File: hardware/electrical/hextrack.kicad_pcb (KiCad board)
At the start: 2 copper layers, 50.8 x 54.9 mm, 37 parts, among them SW1 B3U-1000P, U1 USBLC6-2SC6, U2 nRF52840, Y1 32 MHz Crystal

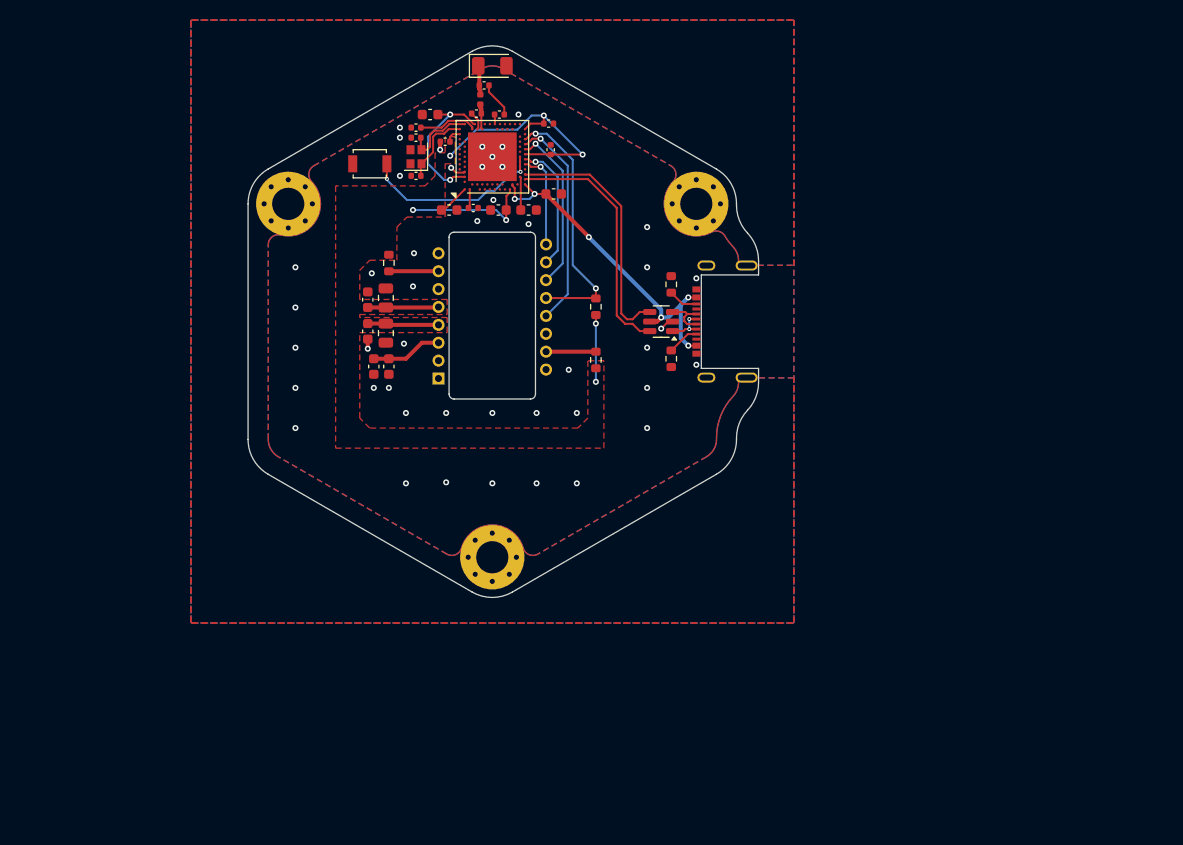
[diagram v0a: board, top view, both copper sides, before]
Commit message: Update schematic to include regulators and switches, update render
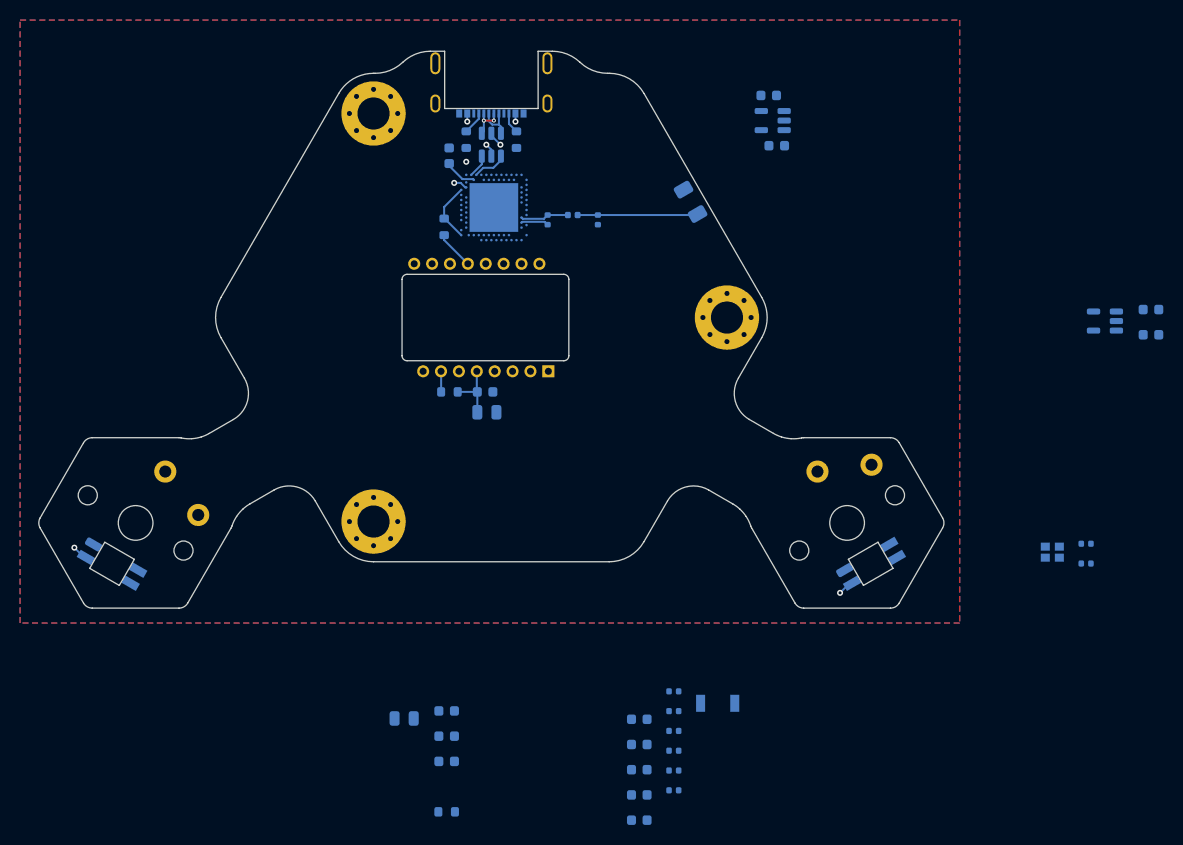
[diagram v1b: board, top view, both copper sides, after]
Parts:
- removed ANT1: Antenna, Diode_SMD:D_1206_3216Metric
- removed NS1: PMW3389DM-T3QU, HexTrack:PixArt_PMW3389DM-T3QU
- removed SW1: B3U-1000P, Button_Switch_SMD:SW_SPST_B3U-1000P
- removed USB1: USB Type-C Receptacle 16P, HexTrack:USB_C_16P_CB0.8_073
- added AN1: Antenna, Diode_SMD:D_1206_3216Metric, B.Cu at (168.3, 93.5)
- added C22: 10uF, Capacitor_SMD:C_0805_2012Metric, B.Cu at (148.1, 114.4)
- added C23: 10uF, Capacitor_SMD:C_0805_2012Metric, B.Cu at (139.8, 144.9)
- added C24: 100nF, Capacitor_SMD:C_0603_1608Metric, B.Cu at (144.1, 144.2)
- added C25: 100nF, Capacitor_SMD:C_0603_1608Metric, B.Cu at (144.1, 146.7)
- added C26: 4.7uF 10V, Capacitor_SMD:C_0603_1608Metric, B.Cu at (144.1, 149.2)
- added D1: SK6812MINI-E, ScottoKeebs_Components:LED_SK6812MINI, F.Cu at (110.8, 129.5)
- added D2: SK6812MINI-E, ScottoKeebs_Components:LED_SK6812MINI, F.Cu at (186.2, 129.5)
- added J1: USB Type-C Receptacle 16P, HexTrack:USB_C_16P_CB0.8_073, B.Cu at (148.5, 77.6)
- added S1: B3U-1000P, Button_Switch_SMD:SW_SPST_B3U-1000P, B.Cu at (171.0, 143.4)
- added S2: Kailh Choc V1, HexTrack:Choc_V1, F.Cu at (113.1, 125.4)
- added S3: Kailh Choc V1, HexTrack:Choc_V1, F.Cu at (183.9, 125.4)
- added U3: AP2204K-3.3, Package_TO_SOT_SMD:SOT-23-5, B.Cu at (209.6, 105.3)
- added U4: nRF52840, HexTrack:Nordic_AQFN-73-1EP_7x7mm_P0.5mm, B.Cu at (148.8, 94.0)
- added U5: PMW3389DM-T3QU, HexTrack:PixArt_PMW3389DM-T3QU, B.Cu at (148.5, 105.0)
- C1, C4: value 100nF -> 1uF; moved to B.Cu
- C10, C11, C14, C15, C19, L1, R3, U1, Y1: moved to B.Cu
- C12: value 100nF -> 4.7uF; footprint Capacitor_SMD:C_0402_1005Metric -> Capacitor_SMD:C_0603_1608Metric; moved to B.Cu
- C13: value 4.7uF -> 100nF; footprint Capacitor_SMD:C_0603_1608Metric -> Capacitor_SMD:C_0402_1005Metric; moved to B.Cu
- C16: value 4.7uF -> 1uF; moved to B.Cu
- C17: value 1uF -> 0.5pF; footprint Capacitor_SMD:C_0603_1608Metric -> Capacitor_SMD:C_0402_1005Metric; moved to B.Cu
- C18: value 12pF -> 0.8pF; moved to B.Cu
- C2, C3: value 10uF -> 1uF; footprint Capacitor_SMD:C_0805_2012Metric -> Capacitor_SMD:C_0603_1608Metric; moved to B.Cu
- C20: value 0.8pF -> 12pF; moved to B.Cu
- C21: value 0.5pF -> 100nF; footprint Capacitor_SMD:C_0402_1005Metric -> Capacitor_SMD:C_0603_1608Metric; moved to B.Cu
- C5: value 100nF -> 4.7uF; moved to B.Cu
- C6: value 4.7uF 10V -> 820pF; footprint Capacitor_SMD:C_0603_1608Metric -> Capacitor_SMD:C_0402_1005Metric; moved to B.Cu
- C7: value 100nF -> 100pF; moved to B.Cu
- C8: value 100pF -> 100nF; moved to B.Cu
- C9: value 820pF -> 4.7uF; footprint Capacitor_SMD:C_0402_1005Metric -> Capacitor_SMD:C_0603_1608Metric; moved to B.Cu
- R1: value 10k -> 5.1k; moved to B.Cu
- R2: value 13R -> 5.1k; moved to B.Cu
- R4: value 5.1k -> 13R; moved to B.Cu
- R5: value 5.1k -> 10k; moved to B.Cu
- U2: value nRF52840 -> AP2204K-1.8; footprint HexTrack:Nordic_AQFN-73-1EP_7x7mm_P0.5mm -> Package_TO_SOT_SMD:SOT-23-5; moved to B.Cu
- moved C4 77.9 mm to (214.1, 106.7), turned to 180 degrees
- moved C3 76.2 mm to (214.1, 104.2), turned to 180 degrees
- moved C19 76.1 mm to (207.7, 127.5)
- moved C20 75.4 mm to (207.7, 129.5), turned to 180 degrees
- moved Y1 74.6 mm to (204.3, 128.3), turned to 180 degrees
- moved C15 68.4 mm to (166.7, 152.1), turned to 180 degrees
- moved C11 68.4 mm to (163.2, 150.0), turned to 180 degrees
- moved C12 67.4 mm to (163.2, 152.5)
- moved C8 65.3 mm to (166.7, 146.1), turned to 180 degrees
- moved C14 63.0 mm to (166.7, 150.1), turned to 180 degrees
- moved C16 62.3 mm to (163.2, 155.0), turned to 180 degrees
- moved C9 61.8 mm to (163.2, 145.0)
- moved C13 56.7 mm to (166.7, 148.1)
- moved C10 54.3 mm to (163.2, 147.5)
- moved C7 53.9 mm to (166.7, 144.2)
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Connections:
- C1 pad 1: +1V8 -> GND
- C1 pad 2: GND -> VBUS
- C10 pad 2: Net-(U2-DECUSB) -> VBUS
- C11 pad 2: Net-(U2-DEC4) -> Net-(U4-DEC4)
- C12 pad 2: +1V8 -> /Block Diagram/MCU/VDD
- C13 pad 2: VBUS -> /Block Diagram/MCU/VDD
- C14 pad 2: +1V8 -> /Block Diagram/MCU/VDD
- C15 pad 2: +1V8 -> /Block Diagram/MCU/VDD
- C16 pad 2: +1V8 -> /Block Diagram/MCU/VDD
- C17 pad 2: +1V8 -> Net-(AN1-A)
- C18 pad 1: Net-(U2-XC1) -> RF_GND
- C18 pad 2: GND -> Net-(U4-ANT)
- C19 pad 1: Net-(U2-XC2) -> Net-(U4-XC1)
- C2 pad 1: +1V8 -> GND
- C2 pad 2: GND -> +1V8
- C20 pad 1: RF_GND -> Net-(U4-XC2)
- C20 pad 2: Net-(U2-ANT) -> GND
- C21 pad 1: GND -> /Block Diagram/MCU/VDD
- C21 pad 2: Net-(ANT1-A) -> GND
- C3 pad 1: +1V8 -> GND
- C3 pad 2: GND -> VBUS
- C4 pad 1: +1V8 -> GND
- C4 pad 2: GND -> +3V3
- C5 pad 1: Net-(NS1-VDDPIX) -> GND
- C5 pad 2: GND -> Net-(U4-DECUSB)
- C6 pad 1: Net-(NS1-VDDPIX) -> GND
- C6 pad 2: GND -> Net-(U4-DEC5)
- C7 pad 2: Net-(U2-DEC1) -> Net-(U4-DEC3)
- C8 pad 2: Net-(U2-DEC3) -> Net-(U4-DEC1)
- C9 pad 2: Net-(U2-DEC5) -> +3V3
- L1 pad 1: Net-(ANT1-A) -> Net-(AN1-A)
- L1 pad 2: Net-(U2-ANT) -> Net-(U4-ANT)
- R1 pad 1: Net-(NS1-~{RESET}) -> GND
- R1 pad 2: +1V8 -> Net-(J1-CC1)
- R2 pad 1: +1V8 -> GND
- R3 pad 1: /Block Diagram/MCU/MISO -> Net-(U5-~{RESET})
- R3 pad 2: +1V8 -> /Block Diagram/MCU/VDD
- R4 pad 1: GND -> +1V8
- R5 pad 1: GND -> /Block Diagram/MCU/MISO
- R5 pad 2: Net-(USB1-CC2) -> /Block Diagram/MCU/VDD
- Y1 pad 1: Net-(U2-XC2) -> Net-(U4-XC2)
- Y1 pad 2: Net-(U2-XC1) -> Net-(U4-XC1)
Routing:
- net +1V8: track 63.5 -> 0.00 mm, vias 7 -> 0
- net VBUS: track 35.3 -> 7.52 mm
- net /Block Diagram/MCU/USB_D-: track 25.0 -> 2.30 mm
- net /Block Diagram/MCU/MISO: track 25.8 -> 3.83 mm, vias 2 -> 0
- net /Block Diagram/MCU/USB_D+: track 25.0 -> 3.46 mm
- net /Block Diagram/MCU/~{CS}: track 21.4 -> 0.00 mm, vias 1 -> 0
- net /Block Diagram/MCU/~{RESET}: track 18.4 -> 0.00 mm, vias 2 -> 0
- net /Block Diagram/MCU/MOSI: track 16.7 -> 0.00 mm, vias 1 -> 0
- net Net-(U2-DEC4): track 14.3 -> 0.00 mm, vias 2 -> 0
- net /Block Diagram/MCU/SCLK: track 13.0 -> 0.00 mm, vias 1 -> 0
- net /Block Diagram/MCU/VDD: track 0.00 -> 12.0 mm
- net Net-(AN1-A): track 0.00 -> 12.0 mm
- net /Block Diagram/MCU/MOTION: track 9.60 -> 0.00 mm, vias 1 -> 0
- net Net-(U2-XC2): track 7.37 -> 0.00 mm
- net Net-(U2-XC1): track 7.29 -> 0.00 mm
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- added copper zone on In2.Cu, net +3V3
- added copper zone on In1.Cu, net VBUS
- removed copper zone on F.Cu, net +1V8
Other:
- board size 50.8 x 54.9 mm -> 90.1 x 55.4 mm
- copper layers 2 -> 4
